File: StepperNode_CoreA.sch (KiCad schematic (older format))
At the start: 1 part

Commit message: First Revision -
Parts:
- gave numbers to parts that had none: 1
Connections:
- net labels added: GNDA, IB_FL_RX_3V, IB_FL_TX, IB_FR_RX_3V, IB_FR_TX, IB_RL_RX_3V, IB_RL_TX
- net labels removed: CHA_IB_FL_NCS, CHA_IB_FL_NIRQ, CHA_IB_FR_NCS, CHA_IB_FR_NIRQ, CHA_IB_RL_NCS, CHA_IB_RL_NIRQ, CHA_SPI_MISO, CHA_SPI_MOSI, CHA_SPI_SCK
- wire segments 40 -> 32
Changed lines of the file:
@@
 Original Author: SafetyLok
 $Comp
-L NODE_CORE_CONNECTOR-RESCUE-rloopStepperNode A?
+L NODE_CORE_CONNECTOR-RESCUE-rloopStepperNode A1
 U 1 1 57538837
 P 8150 4600
-F 0 "A?" H 8600 6000 60  0000 C CNN
+F 0 "A1" H 8600 6000 60  0000 C CNN
 F 1 "NODE_CORE_CONNECTOR" H 8850 3050 60  0000 C CNN
 F 2 "" H 8150 4600 60  0000 C CNN
@@
 Text HLabel 10100 5600 2    60   Output ~ 0
 CHA_DAC_NRST
-Text HLabel 6200 5100 0    60   Input ~ 0
+Text HLabel 6200 5500 0    60   Input ~ 0
 CHA_DAC_NDATA_AVAIL
 Text HLabel 10100 5700 2    60   Output ~ 0
@@
 Text HLabel 10100 5000 2    60   Output ~ 0
 CHA_WDT_PULSE
+Text HLabel 6200 5000 0    60   Output ~ 0
+CHA_AUXPROP_DIR
 Text HLabel 10100 5100 2    60   Input ~ 0
-CHA_IB_FL_NIRQ
+PUSH_INTLK_A
 Text HLabel 10100 5200 2    60   Input ~ 0
-CHA_IB_RL_NIRQ
-Text HLabel 10100 5300 2    60   Input ~ 0
-CHA_IB_FR_NIRQ
-Text HLabel 6200 4700 0    60   Output ~ 0
-CHA_IB_RL_NCS
-Text HLabel 6200 4800 0    60   Output ~ 0
-CHA_IB_FR_NCS
-Text HLabel 6200 4600 0    60   Output ~ 0
-CHA_IB_FL_NCS
-Text HLabel 6200 5500 0    60   Output ~ 0
-CHA_SPI_MOSI
-Text HLabel 6200 5200 0    60   Output ~ 0
-CHA_AUXPROP_DIR
-Text HLabel 6200 5300 0    60   Input ~ 0
-PUSH_INTLK_A
-Text HLabel 6200 5400 0    60   Input ~ 0
 PUSH_INTLK_B
+Text HLabel 6200 4800 0    60   Input ~ 0
+CHA_ACCEL1_NINT
 Text HLabel 6200 4900 0    60   Input ~ 0
-CHA_ACCEL1_NINT
-Text HLabel 6200 5000 0    60   Input ~ 0
 CHA_ACCEL2_NINT
 $Comp
-L +3V3_A #PWR?
+L +3V3_A #PWR22
 U 1 1 575DF18E
 P 8400 3050
-F 0 "#PWR?" H 8400 2900 50  0001 C CNN
+F 0 "#PWR22" H 8400 2900 50  0001 C CNN
 F 1 "+3V3_A" H 8400 3190 50  0000 C CNN
 F 2 "" H 8400 3050 60  0000 C CNN
@@
 $EndComp
 $Comp
-L +5V_A #PWR?
+L +5V_A #PWR20
 U 1 1 575DF1A4
 P 8200 2800
-F 0 "#PWR?" H 8200 2650 50  0001 C CNN
+F 0 "#PWR20" H 8200 2650 50  0001 C CNN
 F 1 "+5V_A" H 8200 2940 50  0000 C CNN
 F 2 "" H 8200 2800 60  0000 C CNN
@@
 $EndComp
 $Comp
-L +24V_A #PWR?
+L +24V_A #PWR18
 U 1 1 575DF1BA
 P 8000 2600
-F 0 "#PWR?" H 8000 2450 50  0001 C CNN
+F 0 "#PWR18" H 8000 2450 50  0001 C CNN
 F 1 "+24V_A" H 8000 2740 50  0000 C CNN
 F 2 "" H 8000 2600 60  0000 C CNN
@@
 	8300 3050 8400 3050
 $Comp
-L GNDD #PWR?
+L GNDD #PWR19
 U 1 1 575DF220
-P 8250 6300
-F 0 "#PWR?" H 8250 6050 50  0001 C CNN
-F 1 "GNDD" H 8250 6150 50  0000 C CNN
-F 2 "" H 8250 6300 50  0000 C CNN
-F 3 "" H 8250 6300 50  0000 C CNN
-	1    8250 6300
+P 8050 6300
+F 0 "#PWR19" H 8050 6050 50  0001 C CNN
+F 1 "GNDD" H 8050 6150 50  0000 C CNN
+F 2 "" H 8050 6300 50  0000 C CNN
+F 3 "" H 8050 6300 50  0000 C CNN
+	1    8050 6300
 	1    0    0    -1
 $EndComp
-Wire Wire Line
-	8050 6300 8250 6300
 Wire Wire Line
 	7400 4400 6200 4400
@@
 	7400 5500 6200 5500
 Wire Wire Line
-	10100 3600 8900 3600
-Wire Wire Line
-	10100 3700 8900 3700
-Text HLabel 10100 3600 2    60   Input ~ 0
-CHA_SPI_MISO
-Text HLabel 10100 3700 2    60   Output ~ 0
-CHA_SPI_SCK
-Wire Wire Line
 	10100 3800 8900 3800
 Wire Wire Line
 	10100 3900 8900 3900
-Wire Wire Line
-	10100 4000 8900 4000
-Wire Wire Line
-	10100 4100 8900 4100
-Wire Wire Line
-	10100 4200 8900 4200
-Wire Wire Line
-	10100 4300 8900 4300
-Wire Wire Line
-	10100 4400 8900 4400
-Wire Wire Line
-	10100 4500 8900 4500
 Wire Wire Line
 	10100 4600 8900 4600
@@
 Wire Wire Line
 	10100 5200 8900 5200
-Wire Wire Line
-	10100 5300 8900 5300
 Wire Wire Line
 	10100 4700 8900 4700
@@
 Text HLabel 10100 3900 2    60   Input ~ 0
 BRAKE2_MLP_3V
+Text HLabel 6200 5400 0    60   Output ~ 0
+IB_RL_TX
+Text HLabel 6200 5300 0    60   Input ~ 0
+IB_RL_RX_3V
+Text HLabel 6200 4700 0    60   Output ~ 0
+IB_FL_TX
+Text HLabel 6200 4600 0    60   Input ~ 0
+IB_FL_RX_3V
+Text HLabel 6200 5200 0    60   Output ~ 0
+IB_FR_TX
+Text HLabel 6200 5100 0    60   Input ~ 0
+IB_FR_RX_3V
+$Comp
+L GNDA #PWR21
+U 1 1 576218DF
+P 8250 6350
+F 0 "#PWR21" H 8250 6100 50  0001 C CNN
+F 1 "GNDA" H 8250 6200 50  0000 C CNN
+F 2 "" H 8250 6350 50  0000 C CNN
+F 3 "" H 8250 6350 50  0000 C CNN
+	1    8250 6350
+	1    0    0    -1
+$EndComp
+Wire Wire Line
+	8150 6300 8050 6300
+Wire Wire Line
+	8250 6300 8250 6350
 $EndSCHEMATC

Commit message: Fix most ERC warnings (non-connected pins, etc)
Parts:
- A1: symbol NODE_CORE_CONNECTOR-RESCUE-rloopStepperNode -> NODE_CORE_CONNECTOR
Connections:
- net CHA_I2C_SCL: now also A1.T29 (I2C_SCL); no longer A1.~ (ID8)
- net CHA_I2C_SDA: now also A1.T30 (I2C_SDA); no longer A1.~ (ID8)
- no-connect marks 0 -> 10
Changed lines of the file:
@@
 Original Author: SafetyLok
 $Comp
-L NODE_CORE_CONNECTOR-RESCUE-rloopStepperNode A1
+L NODE_CORE_CONNECTOR A1
 U 1 1 57538837
 P 8150 4600
@@
 CHA_ACCEL2_NINT
 $Comp
-L +3V3_A #PWR22
+L +3V3_A #PWR020
 U 1 1 575DF18E
 P 8400 3050
-F 0 "#PWR22" H 8400 2900 50  0001 C CNN
+F 0 "#PWR020" H 8400 2900 50  0001 C CNN
 F 1 "+3V3_A" H 8400 3190 50  0000 C CNN
 F 2 "" H 8400 3050 60  0000 C CNN
@@
 $EndComp
 $Comp
-L +5V_A #PWR20
+L +5V_A #PWR021
 U 1 1 575DF1A4
 P 8200 2800
-F 0 "#PWR20" H 8200 2650 50  0001 C CNN
+F 0 "#PWR021" H 8200 2650 50  0001 C CNN
 F 1 "+5V_A" H 8200 2940 50  0000 C CNN
 F 2 "" H 8200 2800 60  0000 C CNN
@@
 $EndComp
 $Comp
-L +24V_A #PWR18
+L +24V_A #PWR022
 U 1 1 575DF1BA
 P 8000 2600
-F 0 "#PWR18" H 8000 2450 50  0001 C CNN
+F 0 "#PWR022" H 8000 2450 50  0001 C CNN
 F 1 "+24V_A" H 8000 2740 50  0000 C CNN
 F 2 "" H 8000 2600 60  0000 C CNN
@@
 	8300 3050 8400 3050
 $Comp
-L GNDD #PWR19
+L GNDD #PWR023
 U 1 1 575DF220
 P 8050 6300
-F 0 "#PWR19" H 8050 6050 50  0001 C CNN
+F 0 "#PWR023" H 8050 6050 50  0001 C CNN
 F 1 "GNDD" H 8050 6150 50  0000 C CNN
 F 2 "" H 8050 6300 50  0000 C CNN
@@
 IB_FR_RX_3V
 $Comp
-L GNDA #PWR21
+L GNDA #PWR024
 U 1 1 576218DF
 P 8250 6350
-F 0 "#PWR21" H 8250 6100 50  0001 C CNN
+F 0 "#PWR024" H 8250 6100 50  0001 C CNN
 F 1 "GNDA" H 8250 6200 50  0000 C CNN
 F 2 "" H 8250 6350 50  0000 C CNN
@@
 Wire Wire Line
 	8250 6300 8250 6350
+NoConn ~ 8900 3600
+NoConn ~ 8900 3700
+NoConn ~ 8900 4000
+NoConn ~ 8900 4100
+NoConn ~ 8900 4200
+NoConn ~ 8900 4300
+NoConn ~ 8900 4400
+NoConn ~ 8900 4500
+NoConn ~ 8900 5300
+NoConn ~ 8900 5800
 $EndSCHEMATC

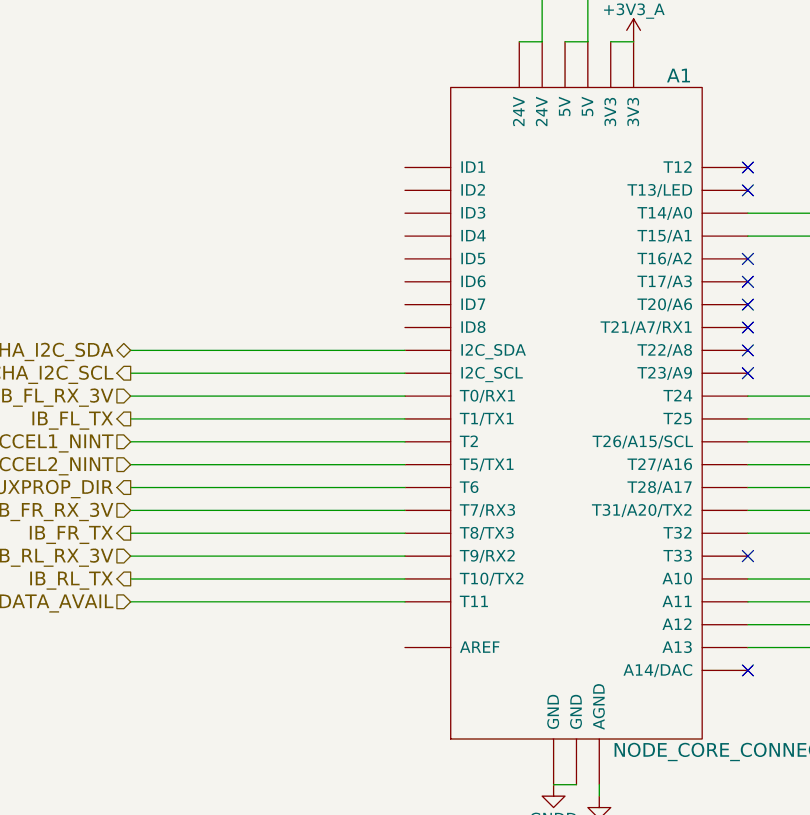
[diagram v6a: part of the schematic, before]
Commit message: Fix further ERC warnings
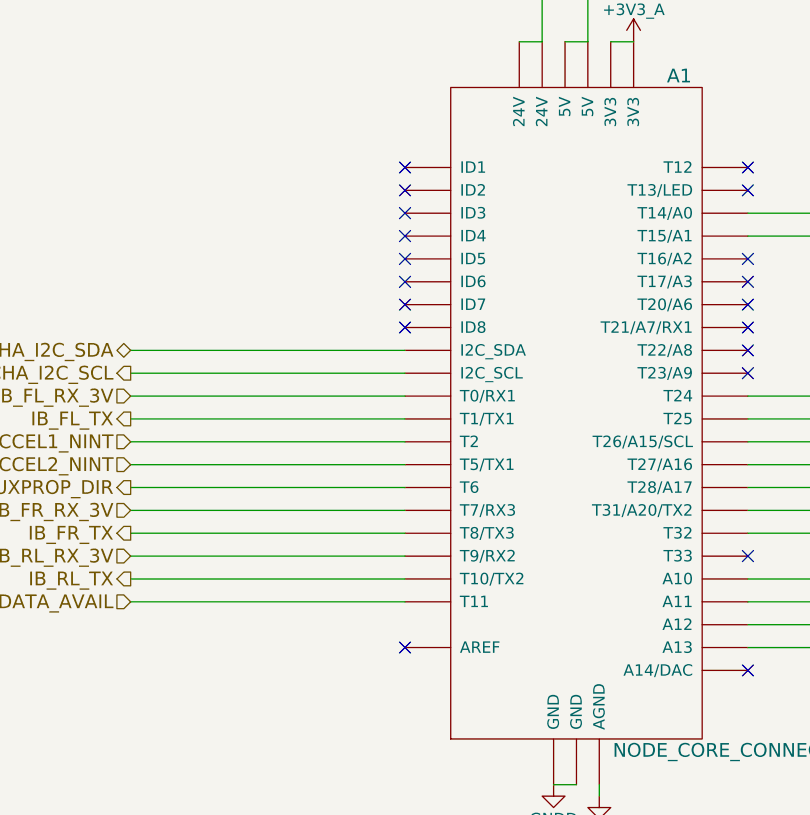
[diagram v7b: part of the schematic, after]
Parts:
- A1: footprint (none) -> footprints:NODECORE
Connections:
- no-connect marks 10 -> 19
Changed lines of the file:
@@
 F 0 "A1" H 8600 6000 60  0000 C CNN
 F 1 "NODE_CORE_CONNECTOR" H 8850 3050 60  0000 C CNN
-F 2 "" H 8150 4600 60  0000 C CNN
+F 2 "footprints:NODECORE" H 8150 4600 60  0001 C CNN
 F 3 "" H 8150 4600 60  0000 C CNN
 	1    8150 4600
@@
 NoConn ~ 8900 5300
 NoConn ~ 8900 5800
+NoConn ~ 7400 3600
+NoConn ~ 7400 3700
+NoConn ~ 7400 3800
+NoConn ~ 7400 3900
+NoConn ~ 7400 4000
+NoConn ~ 7400 4100
+NoConn ~ 7400 4200
+NoConn ~ 7400 4300
+NoConn ~ 7400 5700
 $EndSCHEMATC

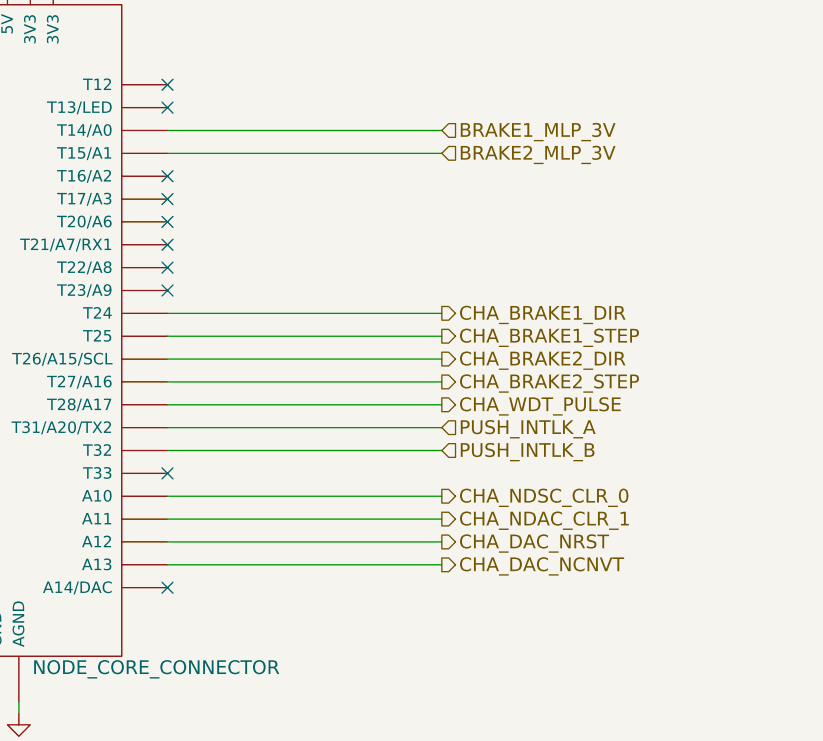
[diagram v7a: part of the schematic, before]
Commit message: Update Teensy IO and place isolation amp.
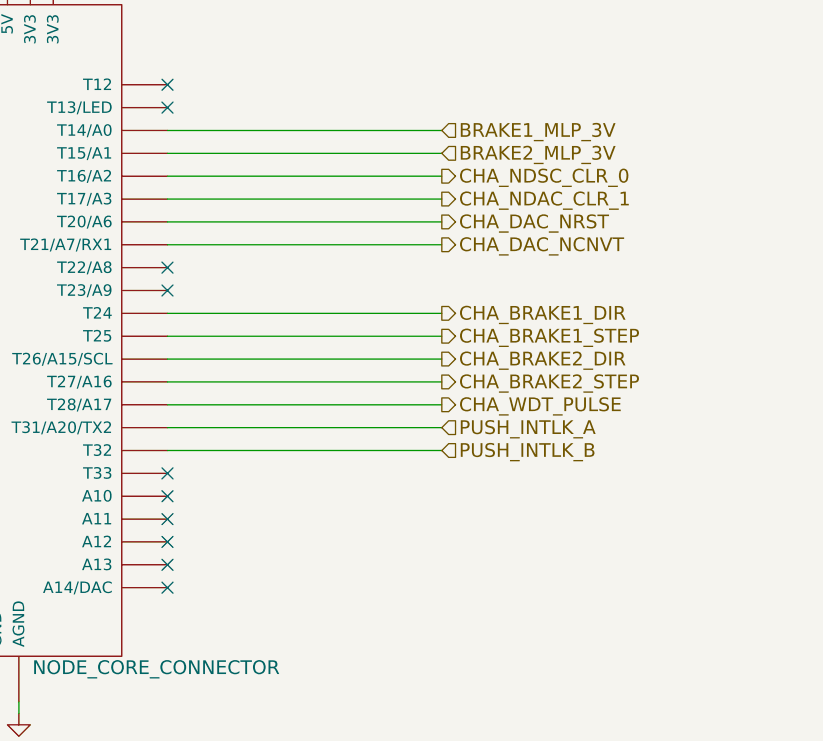
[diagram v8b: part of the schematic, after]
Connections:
- net CHA_DAC_NCNVT: now also A1.T21 (T21/A7/RX1); no longer A1.A13
- net CHA_DAC_NRST: now also A1.T20 (T20/A6); no longer A1.A12
- net CHA_NDAC_CLR_1: now also A1.T17 (T17/A3); no longer A1.A11
- net CHA_NDSC_CLR_0: now also A1.T16 (T16/A2); no longer A1.A10
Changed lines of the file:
@@
 	1    0    0    -1
 $EndComp
-Text HLabel 10100 5400 2    60   Output ~ 0
-CHA_NDSC_CLR_0
-Text HLabel 10100 5500 2    60   Output ~ 0
-CHA_NDAC_CLR_1
-Text HLabel 10100 5600 2    60   Output ~ 0
-CHA_DAC_NRST
 Text HLabel 6200 5500 0    60   Input ~ 0
 CHA_DAC_NDATA_AVAIL
-Text HLabel 10100 5700 2    60   Output ~ 0
-CHA_DAC_NCNVT
 Text HLabel 10100 4600 2    60   Output ~ 0
 CHA_BRAKE1_DIR
@@
 	10100 5000 8900 5000
 Wire Wire Line
-	10100 5500 8900 5500
-Wire Wire Line
-	10100 5600 8900 5600
-Wire Wire Line
-	10100 5700 8900 5700
-Wire Wire Line
-	10100 5400 8900 5400
-Wire Wire Line
 	7400 4900 6200 4900
 Wire Wire Line
@@
 NoConn ~ 8900 3600
 NoConn ~ 8900 3700
-NoConn ~ 8900 4000
-NoConn ~ 8900 4100
-NoConn ~ 8900 4200
-NoConn ~ 8900 4300
 NoConn ~ 8900 4400
 NoConn ~ 8900 4500
@@
 NoConn ~ 7400 4300
 NoConn ~ 7400 5700
+Text HLabel 10100 4000 2    60   Output ~ 0
+CHA_NDSC_CLR_0
+Text HLabel 10100 4100 2    60   Output ~ 0
+CHA_NDAC_CLR_1
+Wire Wire Line
+	10100 4100 8900 4100
+Wire Wire Line
+	10100 4000 8900 4000
+Text HLabel 10100 4200 2    60   Output ~ 0
+CHA_DAC_NRST
+Text HLabel 10100 4300 2    60   Output ~ 0
+CHA_DAC_NCNVT
+Wire Wire Line
+	10100 4200 8900 4200
+Wire Wire Line
+	10100 4300 8900 4300
+NoConn ~ 8900 5400
+NoConn ~ 8900 5500
+NoConn ~ 8900 5600
+NoConn ~ 8900 5700
 $EndSCHEMATC
